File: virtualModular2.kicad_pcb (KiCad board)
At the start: 2 copper layers, 100 x 164 mm, 125 parts, among them CON1 BARREL_JACK, P1 POWER, P18 3VI2C, P19 PIGPIO, P2 FTDI, P3 5V SPI, P4 I2C, Q1 BSS138, Q2 BSS138, SW10 SW_PUSH, SW11 SW_PUSH, SW12 SW_PUSH, SW13 SW_PUSH, SW14 SW_PUSH, SW2 ROTARY_ENCODER_SWITCH, SW3 SW_PUSH, SW4 SW_PUSH, SW5 SW_PUSH, SW6 SW_PUSH, SW7 SW_PUSH, SW8 SW_PUSH, SW9 SW_PUSH, U1 NCP1117ST50T3G

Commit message: details in layout etc
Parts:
- P19: footprint lib_fp:Pin_Header_Straight_2x05_Pitch2.54mm_SMD-raspi -> SparkFun-Connectors:2X5_NOSILK
- moved C1 52.1 mm to (59.0, 14.5)
- moved R1 2.33 mm to (6.00, 25.0), turned to 0 degrees
- moved D2 1.02 mm to (6.00, 19.5)
- moved P2 0.73 mm to (74.3, 25.5)
- moved RV1 0.20 mm to (8.50, 12.4)
- renumbered REF** to HOLE00, REF** to HOLE01, REF** to HOLE02, REF** to HOLE03, REF** to HOLE04, REF** to HOLE05, REF** to HOLE06, REF** to HOLE07, REF** to HOLE08, REF** to HOLE09, REF** to HOLE10, REF** to HOLE11, REF** to HOLE12, REF** to HOLE13, REF** to HOLE14, REF** to HOLE15, REF** to HOLE16, REF** to HOLE17, REF** to HOLE18, REF** to HOLE19, REF** to HOLE20, REF** to HOLE21, REF** to HOLE22, REF** to HOLE23
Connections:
- SW2 pad A: (no net) -> /ENCA

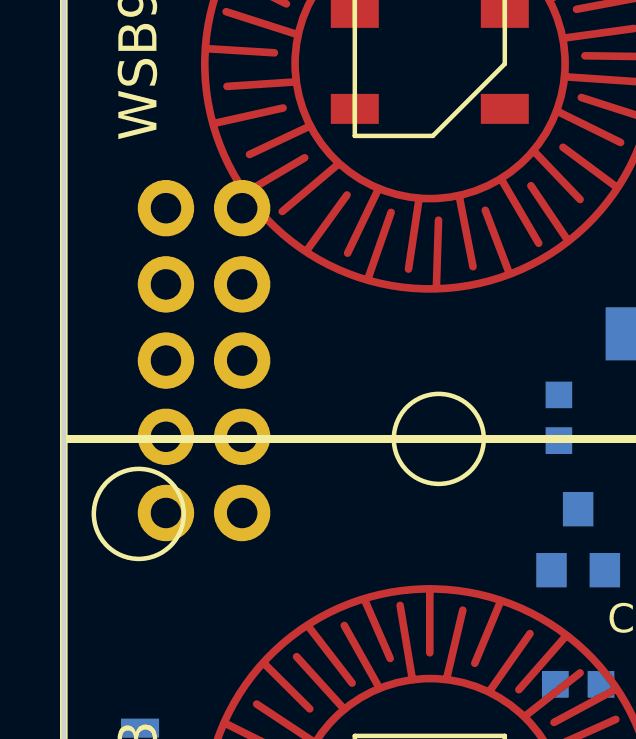
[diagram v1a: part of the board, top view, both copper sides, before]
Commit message: PIGPIO was right over a button pad
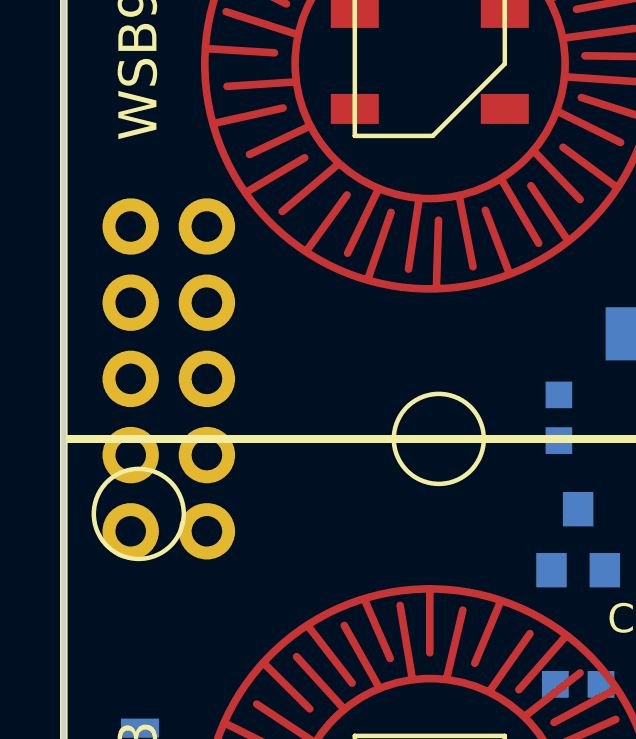
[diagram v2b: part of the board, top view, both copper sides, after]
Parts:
- moved P19 1.32 mm to (3.50, 73.0)
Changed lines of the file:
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@@
     (links 284)
     (no_connects 284)
-    (area -0.075001 -0.075001 100.075001 164.075001)
+    (area -9.7188 -1.72 104.914286 176.198)
     (thickness 1.6)
     (drawings 17)
@@
   )
   (module SparkFun-Connectors:2X5_NOSILK (layer B.Cu)
-    (at 4.675 72.39)
+    (at 3.5 73)
     (fp_text reference P19 (at 2.793291 3.322477 90) (layer B.SilkS)
       (effects (font (size 0.38608 0.38608) (thickness 0.032512)) (justify left bottom mirror))
@@
   )
   (module SeeedOPL-Capacitor:C0402 (layer B.Cu)
-    (at 59.03772 14.5 90)
+    (at 59.0377 14.5 90)
     (descr 0402)
     (tags 0402)
@@
   )
   (module lib_fp:trimpot (layer B.Cu)
-    (at 8.49892 12.4 90)
+    (at 8.4989 12.4 90)
     (attr virtual)
     (fp_text reference RV1 (at -0.05 -1.35 90) (layer B.SilkS)

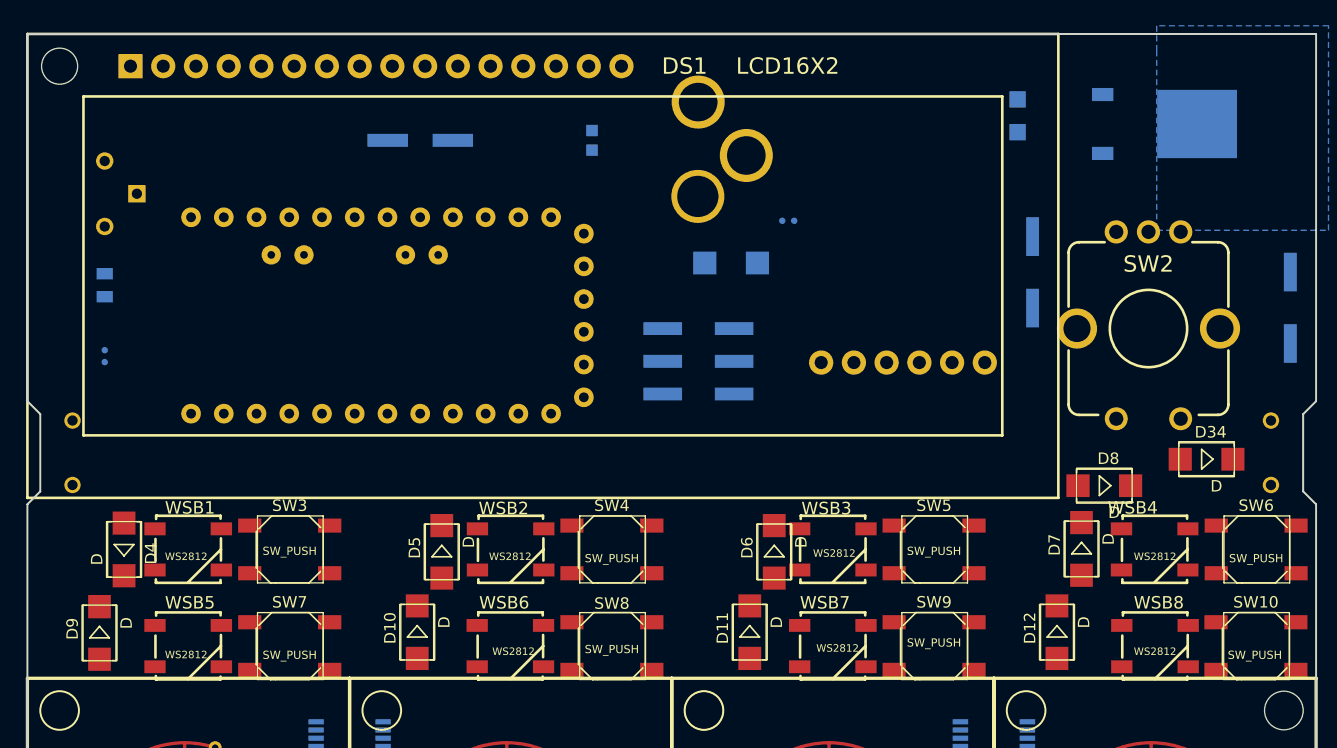
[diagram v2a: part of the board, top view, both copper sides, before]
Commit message: repositioning some items
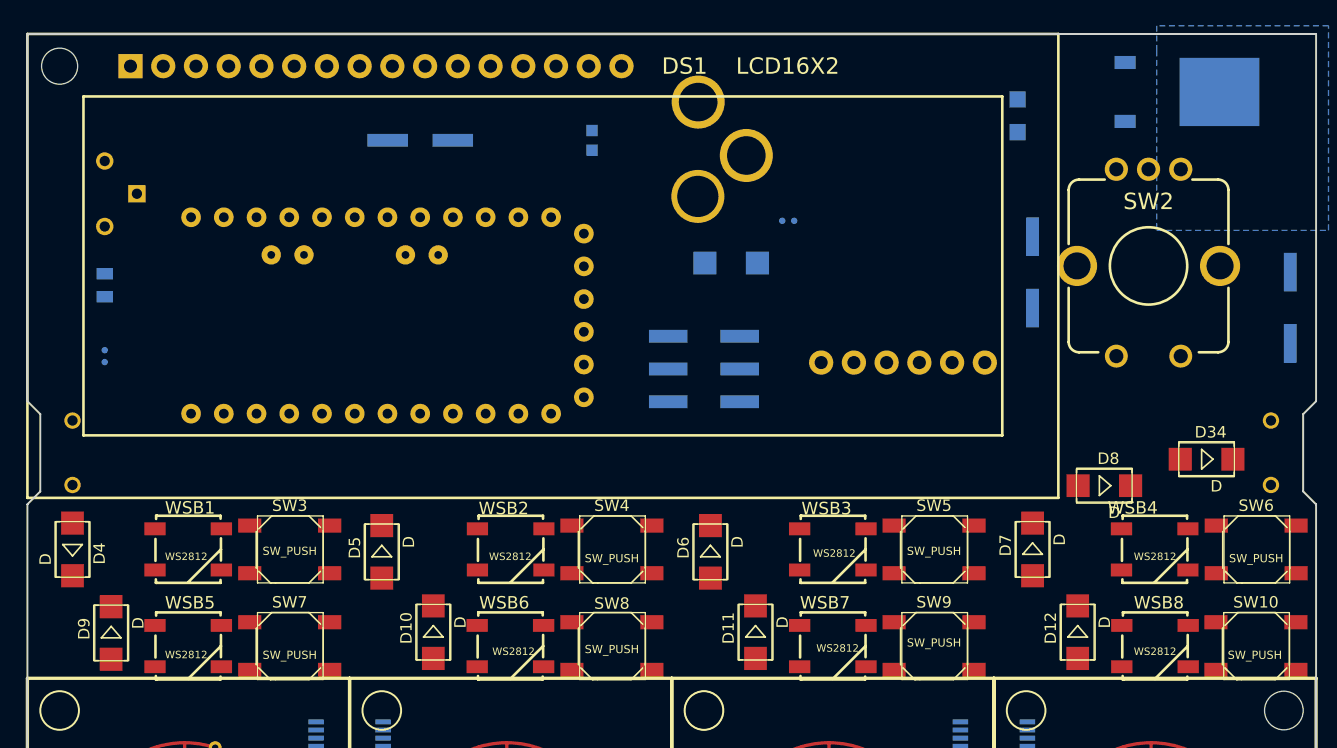
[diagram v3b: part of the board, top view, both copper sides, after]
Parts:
- moved D6 4.95 mm to (53.0, 40.2)
- moved SW2 4.86 mm to (87.0, 18.0)
- moved D5 4.66 mm to (27.5, 40.2)
- moved D4 4.00 mm to (3.50, 40.0)
- moved D7 3.80 mm to (78.0, 40.0)
- moved U1 3.03 mm to (90.0, 4.50)
- moved D12 1.61 mm to (81.5, 46.4)
- moved D10 1.25 mm to (31.5, 46.4)
- moved D9 0.91 mm to (6.50, 46.5)
- moved P3 0.74 mm to (52.5, 26.0)
- moved D11 0.45 mm to (56.5, 46.4)
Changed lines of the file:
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@@
     (38 B.Mask user)
     (39 F.Mask user)
-    (40 Dwgs.User user)
+    (40 Dwgs.User user hide)
     (41 Cmts.User user)
     (42 Eco1.User user)
@@
   )
   (module SparkFun-Electromechanical:ENCODER_LED_2 (layer F.Cu)
-    (at 86.995 22.86 180)
+    (at 87 18 180)
     (descr "<h3>2-color Illuminated Rotary Encoder</h3>")
     (fp_text reference SW2 (at 0 5 180) (layer F.SilkS)
       (effects (font (thickness 0.15)))
     )
-    (fp_text value ROTARY_ENCODER_SWITCH (at 0 0 180) (layer F.SilkS) hide
+    (fp_text value ROTARY_ENCODER_SWITCH (at 0 3 180) (layer F.SilkS) hide
       (effects (font (thickness 0.15)))
     )
@@
   )
   (module SeeedOPL-IC:TO-252 (layer B.Cu)
-    (at 88.265 6.985 90)
+    (at 90 4.5 90)
     (descr "SMALL OUTLINE TRANSISTOR")
     (tags "SMALL OUTLINE TRANSISTOR")
@@
   )
   (module Pin_Headers:Pin_Header_Straight_2x03_Pitch2.54mm_SMD (layer B.Cu)
-    (at 52.07 25.4)
+    (at 52.5 26)
     (descr "surface-mounted straight pin header, 2x03, 2.54mm pitch, double rows")
     (tags "Surface mounted pin header SMD 2x03 2.54mm double row")
@@
   )
   (module lib_fp:DO-214AC (layer F.Cu)
-    (at 7.5 40 270)
+    (at 3.5 40 270)
     (descr HTTP://WWW.SYCELECTRONICA.COM.AR/SEMICONDUCTORES/1N4007-SMD.PDF)
     (tags HTTP://WWW.SYCELECTRONICA.COM.AR/SEMICONDUCTORES/1N4007-SMD.PDF)
@@
   )
   (module lib_fp:DO-214AC (layer F.Cu)
-    (at 32.155 40.19 90)
+    (at 27.5 40.19 90)
     (descr HTTP://WWW.SYCELECTRONICA.COM.AR/SEMICONDUCTORES/1N4007-SMD.PDF)
     (tags HTTP://WWW.SYCELECTRONICA.COM.AR/SEMICONDUCTORES/1N4007-SMD.PDF)
@@
   )
   (module lib_fp:DO-214AC (layer F.Cu)
-    (at 57.955 40.19 90)
+    (at 53 40.19 90)
     (descr HTTP://WWW.SYCELECTRONICA.COM.AR/SEMICONDUCTORES/1N4007-SMD.PDF)
     (tags HTTP://WWW.SYCELECTRONICA.COM.AR/SEMICONDUCTORES/1N4007-SMD.PDF)
@@
   )
   (module lib_fp:DO-214AC (layer F.Cu)
-    (at 81.8 39.9604 90)
+    (at 78 40 90)
     (descr HTTP://WWW.SYCELECTRONICA.COM.AR/SEMICONDUCTORES/1N4007-SMD.PDF)
     (tags HTTP://WWW.SYCELECTRONICA.COM.AR/SEMICONDUCTORES/1N4007-SMD.PDF)
@@
   )
   (module lib_fp:DO-214AC (layer F.Cu)
-    (at 5.595 46.48 90)
+    (at 6.5 46.48 90)
     (descr HTTP://WWW.SYCELECTRONICA.COM.AR/SEMICONDUCTORES/1N4007-SMD.PDF)
     (tags HTTP://WWW.SYCELECTRONICA.COM.AR/SEMICONDUCTORES/1N4007-SMD.PDF)
@@
   )
   (module lib_fp:DO-214AC (layer F.Cu)
-    (at 30.25 46.42 90)
+    (at 31.5 46.42 90)
     (descr HTTP://WWW.SYCELECTRONICA.COM.AR/SEMICONDUCTORES/1N4007-SMD.PDF)
     (tags HTTP://WWW.SYCELECTRONICA.COM.AR/SEMICONDUCTORES/1N4007-SMD.PDF)
@@
   )
   (module lib_fp:DO-214AC (layer F.Cu)
-    (at 56.05 46.42 90)
+    (at 56.5 46.42 90)
     (descr HTTP://WWW.SYCELECTRONICA.COM.AR/SEMICONDUCTORES/1N4007-SMD.PDF)
     (tags HTTP://WWW.SYCELECTRONICA.COM.AR/SEMICONDUCTORES/1N4007-SMD.PDF)
@@
   )
   (module lib_fp:DO-214AC (layer F.Cu)
-    (at 79.895 46.42 90)
+    (at 81.5 46.42 90)
     (descr HTTP://WWW.SYCELECTRONICA.COM.AR/SEMICONDUCTORES/1N4007-SMD.PDF)
     (tags HTTP://WWW.SYCELECTRONICA.COM.AR/SEMICONDUCTORES/1N4007-SMD.PDF)
@@
     (fp_line (start -2 -2.675) (end 2 -2.675) (layer B.SilkS) (width 0.15))
     (fp_line (start -3.275 2.725) (end 2 2.725) (layer B.SilkS) (width 0.15))
-    (fp_text user %R (at 0 -0.1) (layer B.Fab)
+    (fp_text user %R (at 0 -4.6) (layer B.Fab)
       (effects (font (size 0.8 0.8) (thickness 0.15)) (justify mirror))
     )
@@
       (effects (font (size 1 1) (thickness 0.15)) (justify mirror))
     )
-    (fp_text value 4051 (at 0 3.6 180) (layer B.Fab)
+    (fp_text value 4051 (at 0 3.5 180) (layer B.Fab)
       (effects (font (size 1 1) (thickness 0.15)) (justify mirror))
     )
@@
     (fp_line (start -2 -2.675) (end 2 -2.675) (layer B.SilkS) (width 0.15))
     (fp_line (start -3.275 2.725) (end 2 2.725) (layer B.SilkS) (width 0.15))
-    (fp_text user %R (at -0.21 0.1 180) (layer B.Fab)
+    (fp_text user %R (at 0 4.6 180) (layer B.Fab)
       (effects (font (size 0.8 0.8) (thickness 0.15)) (justify mirror))
     )

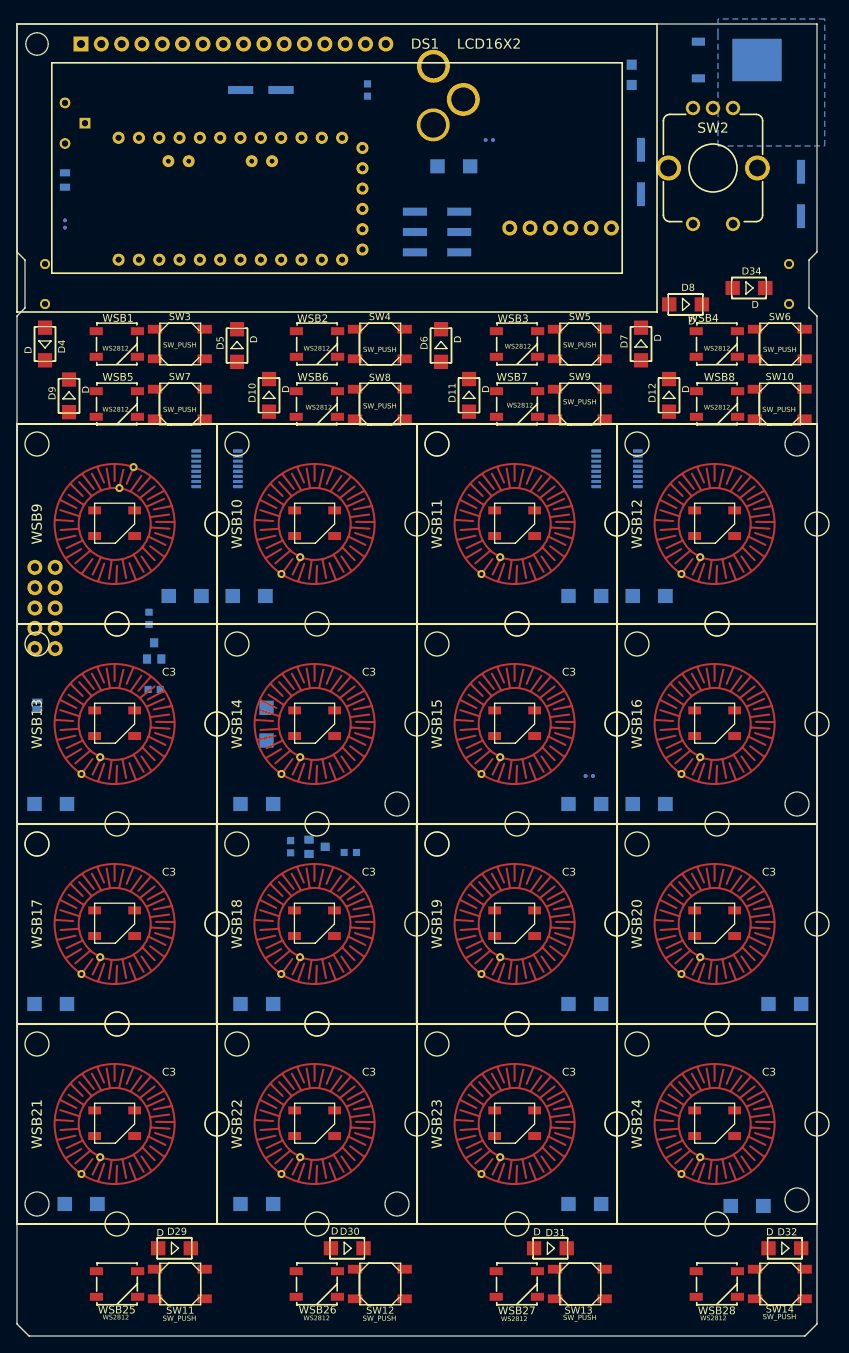
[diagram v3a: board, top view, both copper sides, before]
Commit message: Add pulldown resistor to MUXA, and test routing, small changes
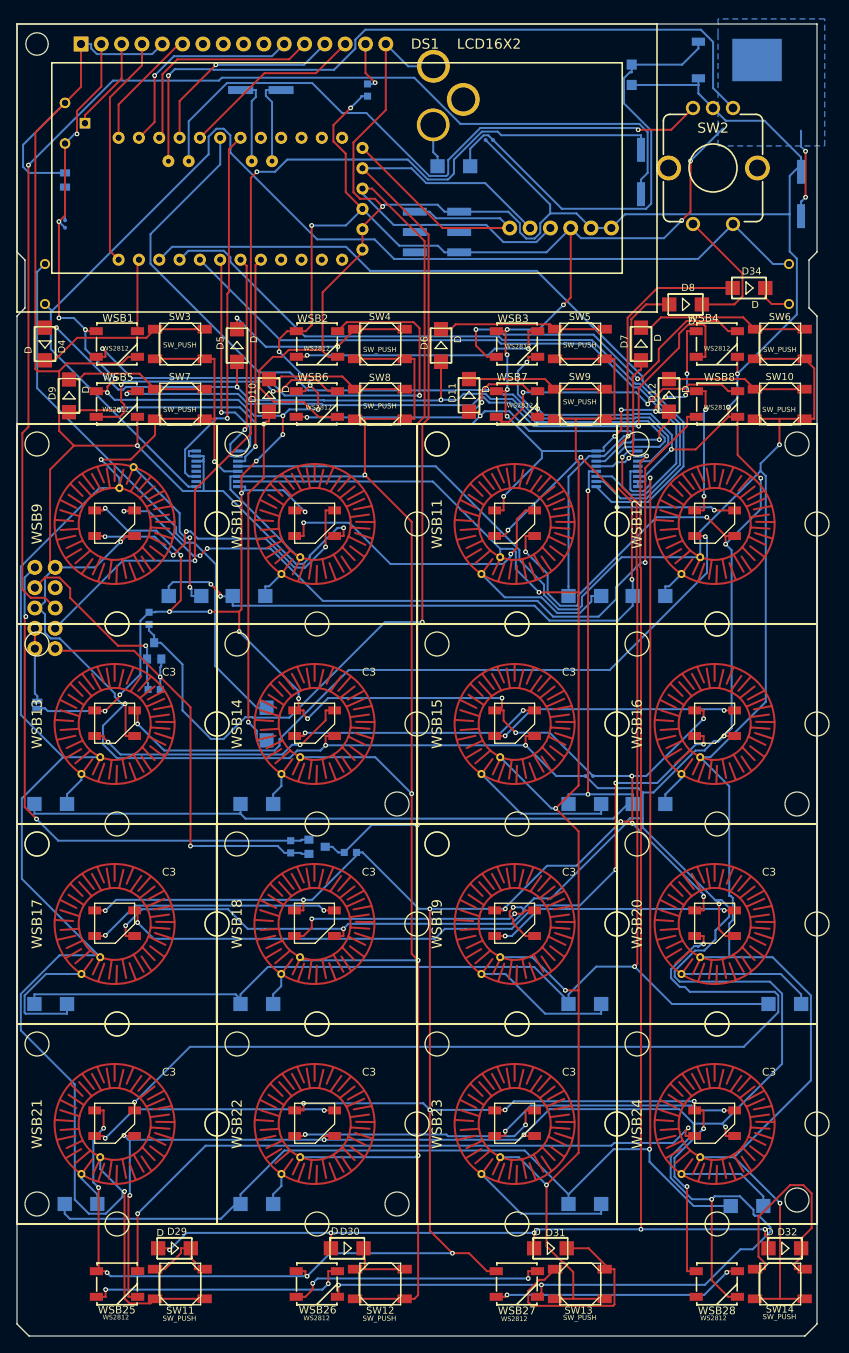
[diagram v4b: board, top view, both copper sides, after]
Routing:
- net GND: track 0.00 -> 1009.3 mm, vias 0 -> 29
- net +5V: track 0.00 -> 786.1 mm, vias 0 -> 65
- net /MUXAX3: track 0.00 -> 250.8 mm, vias 0 -> 2
- net /MUXAX2: track 0.00 -> 223.2 mm, vias 0 -> 4
- net /MUXAX1: track 0.00 -> 219.0 mm, vias 0 -> 4
- net /MUXAX0: track 0.00 -> 201.9 mm, vias 0 -> 3
- net /MUXBX5: track 0.00 -> 189.8 mm, vias 0 -> 2
- net /MUXBX6: track 0.00 -> 181.6 mm, vias 0 -> 6
- net /MUXBX4: track 0.00 -> 169.0 mm, vias 0 -> 2
- net /PI_SCL: track 0.00 -> 151.3 mm, vias 0 -> 1
- net /MUXAX4: track 0.00 -> 146.1 mm
- net /MUXBX2: track 0.00 -> 139.7 mm, vias 0 -> 4
- net /PI5vTX0: track 0.00 -> 135.1 mm, vias 0 -> 1
- net /MUXBX1: track 0.00 -> 133.0 mm, vias 0 -> 5
- net /MUXBX3: track 0.00 -> 130.3 mm, vias 0 -> 2
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
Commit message: shematic addition of midi io (to be an optional later)
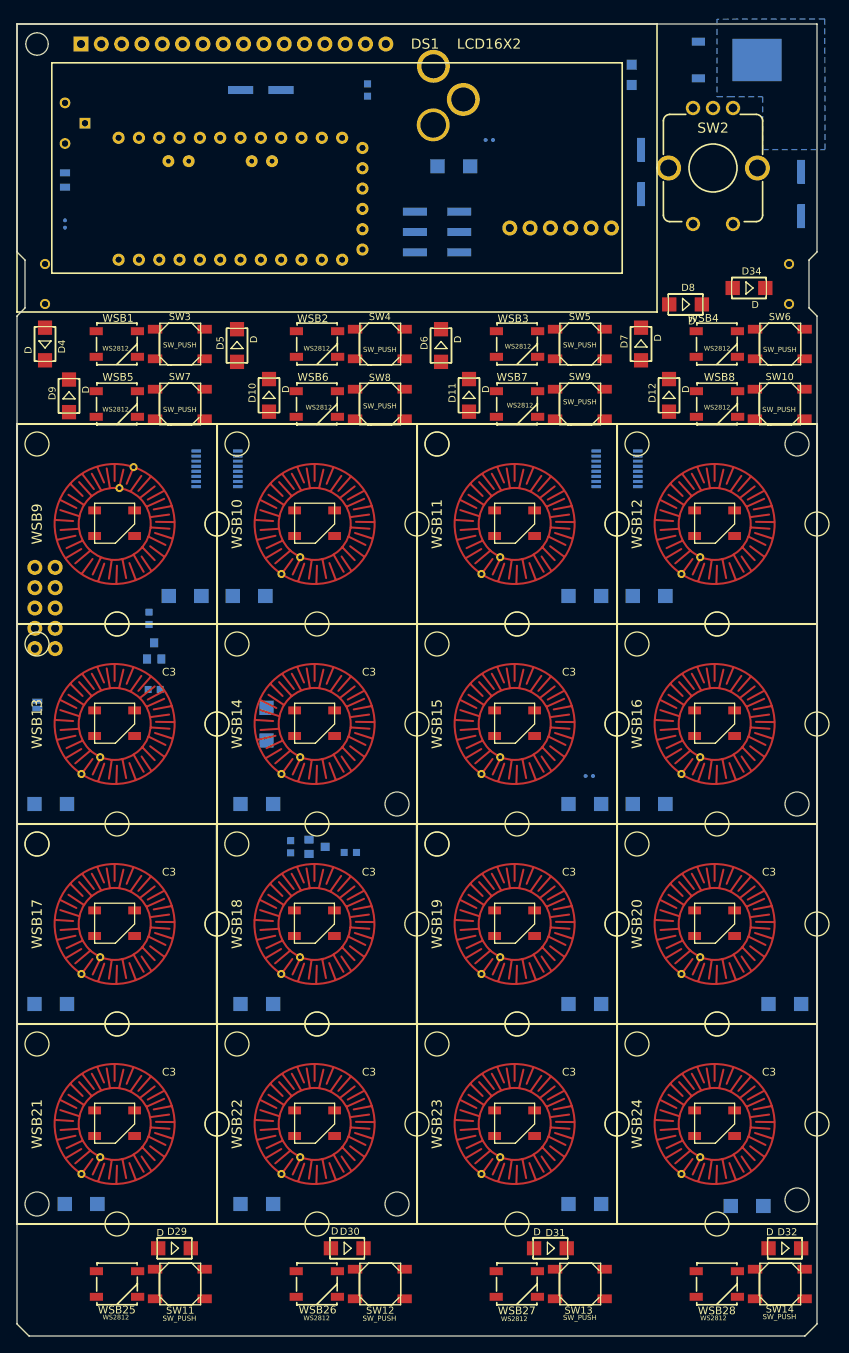
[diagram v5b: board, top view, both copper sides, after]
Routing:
- net GND: track 1009.3 -> 0.00 mm, vias 29 -> 0
- net +5V: track 786.1 -> 0.00 mm, vias 65 -> 0
- net /MUXAX3: track 250.8 -> 0.00 mm, vias 2 -> 0
- net /MUXAX2: track 223.2 -> 0.00 mm, vias 4 -> 0
- net /MUXAX1: track 219.0 -> 0.00 mm, vias 4 -> 0
- net /MUXAX0: track 201.9 -> 0.00 mm, vias 3 -> 0
- net /MUXBX5: track 189.8 -> 0.00 mm, vias 2 -> 0
- net /MUXBX6: track 181.6 -> 0.00 mm, vias 6 -> 0
- net /MUXBX4: track 169.0 -> 0.00 mm, vias 2 -> 0
- net /PI_SCL: track 151.3 -> 0.00 mm, vias 1 -> 0
- net /MUXAX4: track 146.1 -> 0.00 mm
- net /MUXBX2: track 139.7 -> 0.00 mm, vias 4 -> 0
- net /PI5vTX0: track 135.1 -> 0.00 mm, vias 1 -> 0
- net /MUXBX1: track 133.0 -> 0.00 mm, vias 5 -> 0
- net /MUXBX3: track 130.3 -> 0.00 mm, vias 2 -> 0
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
